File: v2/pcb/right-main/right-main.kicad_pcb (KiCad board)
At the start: 2 copper layers, 83 x 79 mm, 33 parts, among them J1 Conn_01x10, SW1 SW_Push, SW10 SW_Push, SW11 SW_Push, SW12 SW_Push, SW13 SW_Push, SW14 SW_Push, SW15 SW_Push, SW16 SW_Push, SW2 SW_Push, SW3 SW_Push, SW4 SW_Push, SW5 SW_Push, SW6 SW_Push, SW7 SW_Push, SW8 SW_Push, SW9 SW_Push

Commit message: feat: update case data
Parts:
- moved D10 69.8 mm to (198.7, 110.5), turned to 0 degrees
- moved D5 69.0 mm to (197.8, 94.5), turned to 0 degrees
- moved D15 64.0 mm to (193.0, 131.7), turned to 90 degrees
- moved D16 64.0 mm to (193.0, 147.7), turned to 90 degrees
- moved D11 64.0 mm to (129.0, 123.5), turned to 90 degrees
- moved SW1 64.0 mm to (134.0, 91.5), turned to -90 degrees
- moved SW10 64.0 mm to (198.0, 115.5), turned to -90 degrees
- moved SW11 64.0 mm to (134.0, 123.5), turned to 90 degrees
- moved SW15 64.0 mm to (198.0, 131.5), turned to 90 degrees
- moved SW16 64.0 mm to (198.0, 147.5), turned to 90 degrees
- moved SW5 64.0 mm to (198.0, 99.5), turned to -90 degrees
- moved SW6 64.0 mm to (134.0, 107.5), turned to -90 degrees
- moved D1 59.4 mm to (133.8, 86.5), turned to 0 degrees
- moved D6 59.2 mm to (134.0, 102.5), turned to 0 degrees
- moved J1 55.9 mm to (142.2, 93.8)
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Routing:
- net /COL4: track 0.00 -> 108.2 mm
- net /ROW2: track 0.00 -> 105.9 mm, vias 0 -> 6
- net /ROW1: track 0.00 -> 84.2 mm, vias 0 -> 6
- net /ROW0: track 0.00 -> 82.7 mm, vias 0 -> 6
- net /ROW3: track 0.00 -> 76.0 mm, vias 0 -> 2
- net /COL3: track 0.00 -> 71.3 mm
- net /COL1: track 0.00 -> 58.5 mm
- net /COL2: track 0.00 -> 54.1 mm
- net /COL0: track 0.00 -> 36.1 mm
- net Net-(D2-K): track 0.00 -> 10.5 mm
- net Net-(D1-K): track 0.00 -> 8.42 mm
- net Net-(D5-K): track 0.00 -> 8.42 mm
- net Net-(D7-K): track 0.00 -> 8.27 mm
- net Net-(D6-K): track 0.00 -> 8.27 mm
- net Net-(D4-K): track 0.00 -> 8.27 mm
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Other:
- outline, holes or cut-outs redrawn

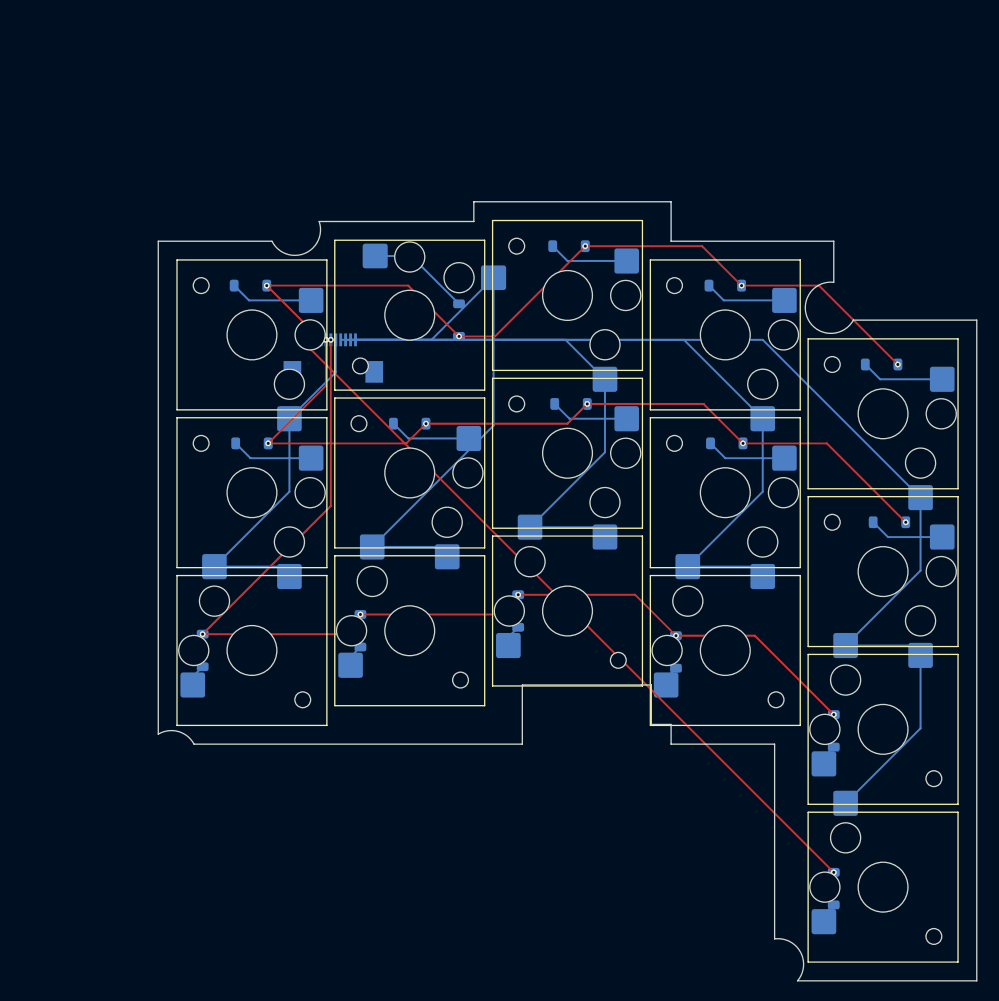
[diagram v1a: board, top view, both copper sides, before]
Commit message: feat: add right main pcb
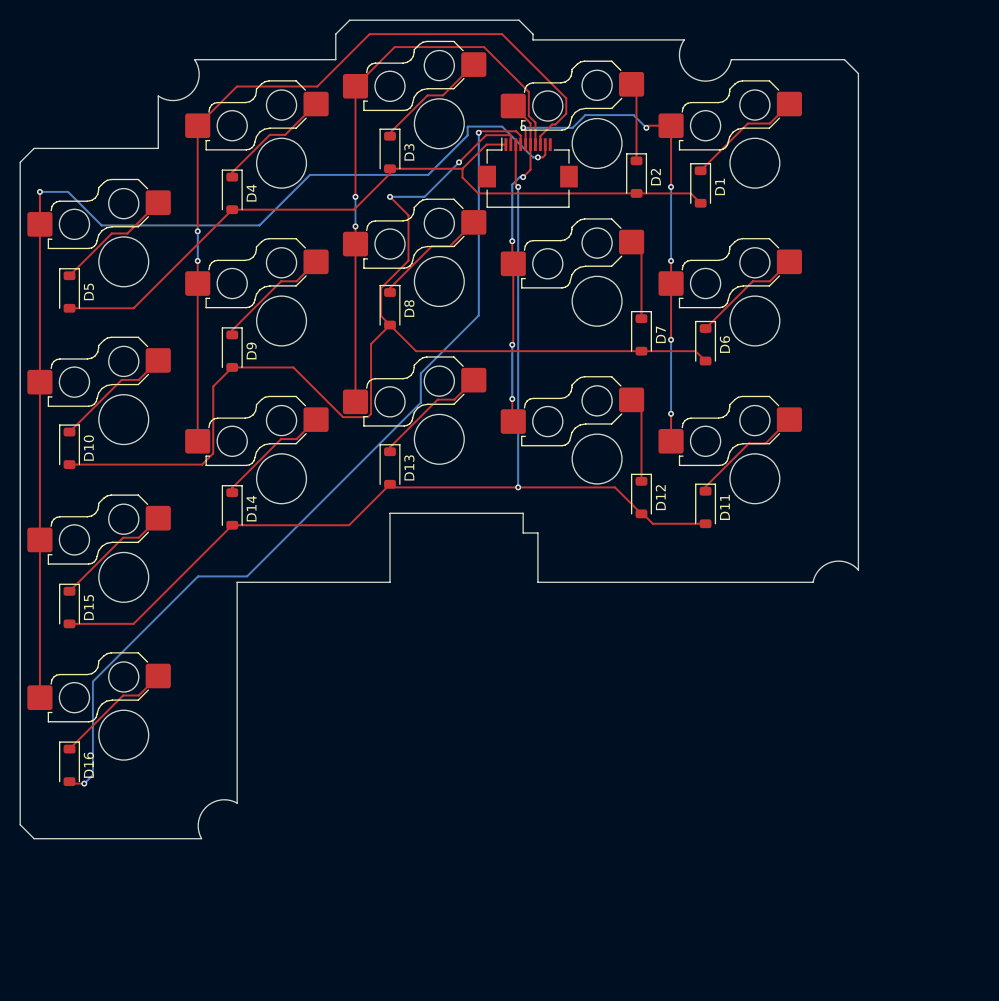
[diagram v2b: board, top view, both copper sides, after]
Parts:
- D1, D10, D11, D12, D13, D14, D15, D16, D2, D3, D4, D5, D6, D7, D8, D9, J1: moved to F.Cu
- SW1, SW10, SW11, SW12, SW13, SW14, SW15, SW16, SW2, SW3, SW4, SW5, SW6, SW7, SW8, SW9: moved to B.Cu
- moved D10 83.5 mm to (115.5, 103.0), turned to -90 degrees
- moved D5 82.7 mm to (115.5, 87.2), turned to -90 degrees
- moved SW16 78.5 mm to (121.0, 132.1), turned to 180 degrees
- moved SW10 78.5 mm to (121.0, 100.1), turned to 180 degrees
- moved SW15 78.5 mm to (121.0, 116.1), turned to 180 degrees
- moved SW5 78.5 mm to (121.0, 84.1), turned to 180 degrees
- moved D15 78.5 mm to (115.5, 119.2), turned to -90 degrees
- moved D16 78.5 mm to (115.5, 135.2), turned to -90 degrees
- moved SW1 53.9 mm to (185.0, 74.1), turned to 180 degrees
- moved SW11 53.9 mm to (185.0, 106.1), turned to 180 degrees
- moved SW6 53.9 mm to (185.0, 90.1), turned to 180 degrees
- moved D11 53.0 mm to (180.0, 109.0), turned to -90 degrees
- moved D9 51.0 mm to (132.0, 93.2), turned to -90 degrees
- moved D4 50.9 mm to (132.0, 77.2), turned to -90 degrees
- moved SW14 48.3 mm to (137.0, 106.1), turned to 180 degrees
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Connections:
- J1 pad 1: /COL4 -> /ROW0
- J1 pad 10: /ROW3 -> unconnected-(J1-Pin_10-Pad10)
- J1 pad 2: /COL3 -> /ROW1
- J1 pad 3: /COL2 -> /ROW2
- J1 pad 4: /COL1 -> /ROW3
- J1 pad 6: /ROW2 -> /COL1
- J1 pad 7: /ROW1 -> /COL2
- J1 pad 8: /ROW0 -> /COL3
- J1 pad 9: GND -> /COL4
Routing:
- net /ROW1: track 84.2 -> 115.2 mm, vias 6 -> 2
- net /COL1: track 58.5 -> 33.8 mm, vias 0 -> 4
- net /ROW3: track 76.0 -> 92.5 mm
- net /COL0: track 36.1 -> 50.0 mm, vias 0 -> 6
- net /COL3: track 71.3 -> 81.9 mm, vias 0 -> 2
- net Net-(D16-K): track 2.11 -> 12.1 mm
- net Net-(D15-K): track 2.11 -> 12.1 mm
- net Net-(D14-K): track 2.11 -> 11.9 mm
- net Net-(D13-K): track 2.26 -> 11.8 mm
- net Net-(D11-K): track 2.26 -> 11.8 mm
- net Net-(D12-K): track 2.26 -> 8.68 mm
- net /ROW0: track 82.7 -> 77.5 mm, vias 6 -> 0
- net /COL2: track 54.1 -> 58.7 mm, vias 0 -> 2
- net Net-(D10-K): track 7.62 -> 12.0 mm
- net Net-(D8-K): track 7.92 -> 11.7 mm
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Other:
- board size 83 x 79 mm -> 85 x 83 mm
